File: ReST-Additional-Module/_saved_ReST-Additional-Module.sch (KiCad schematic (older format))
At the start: 11 parts, among them P1 CONN_02X06, P2 02-SCREW-TERM, P3 02-SCREW-TERM, Q1 Q_BSH105, Q2 Q_AOT240L

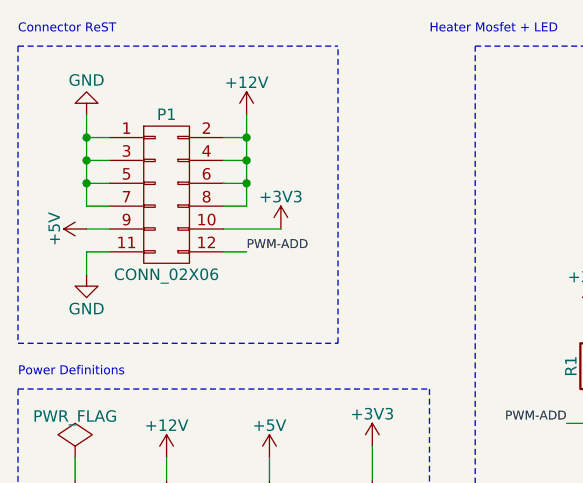
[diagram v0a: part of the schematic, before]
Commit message: Added Additional Module
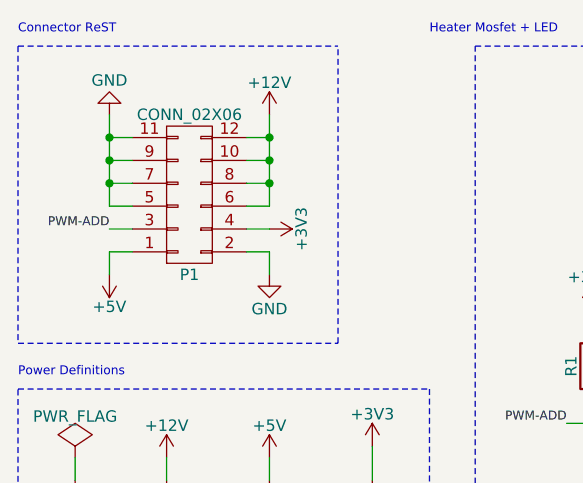
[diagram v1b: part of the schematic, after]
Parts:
- P1: footprint (none) -> Pin_Headers:Pin_Header_Angled_2x06
- P2: footprint 5mm-pitch-terminal:mkds_1,5-2 -> Pin_Headers:Pin_Header_Straight_1x02
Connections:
- net +12V: now also P1.10 (P10), P1.12 (P12); no longer P1.2 (P2), P1.4 (P4)
- net +3V3: now also P1.4 (P4); no longer P1.10 (P10)
- net +5V: now also P1.1 (P1); no longer P1.9 (P9)
- net GND: now also P1.2 (P2), P1.9 (P9); no longer P1.1 (P1), P1.3 (P3)
- net PWM-ADD: now also P1.3 (P3); no longer P1.12 (P12)
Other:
- moved on the sheet: P1
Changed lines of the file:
@@
 F 0 "P2" H 7350 2850 50  0000 C CNN
 F 1 "02-SCREW-TERM" V 7450 2700 50  0000 C CNN
-F 2 "5mm-pitch-terminal:mkds_1,5-2" H 7350 2700 50  0001 C CNN
+F 2 "Pin_Headers:Pin_Header_Straight_1x02" H 7350 2700 50  0001 C CNN
 F 3 "" H 7350 2700 50  0000 C CNN
 	1    7350 2700
@@
 $EndComp
 $Comp
-L +12V #PWR13
+L +12V #PWR01
 U 1 1 56A6924C
 P 6850 2350
-F 0 "#PWR13" H 6850 2200 50  0001 C CNN
+F 0 "#PWR01" H 6850 2200 50  0001 C CNN
 F 1 "+12V" H 6850 2490 50  0000 C CNN
 F 2 "" H 6850 2350 50  0000 C CNN
@@
 $EndComp
 $Comp
-L +5V #PWR3
+L +5V #PWR02
 U 1 1 56A6A1BB
-P 2950 2900
-F 0 "#PWR3" H 2950 2750 50  0001 C CNN
-F 1 "+5V" H 2950 3040 50  0000 C CNN
-F 2 "" H 2950 2900 50  0000 C CNN
-F 3 "" H 2950 2900 50  0000 C CNN
-	1    2950 2900
-	0    -1   -1   0
-$EndComp
-$Comp
-L +3V3 #PWR8
+P 3050 3100
+F 0 "#PWR02" H 3050 2950 50  0001 C CNN
+F 1 "+5V" H 3050 3240 50  0000 C CNN
+F 2 "" H 3050 3100 50  0000 C CNN
+F 3 "" H 3050 3100 50  0000 C CNN
+	1    3050 3100
+	-1   0    0    1
+$EndComp
+$Comp
+L +3V3 #PWR03
 U 1 1 56A6A1DD
-P 3800 2900
-F 0 "#PWR8" H 3800 2750 50  0001 C CNN
-F 1 "+3V3" H 3800 3040 50  0000 C CNN
-F 2 "" H 3800 2900 50  0000 C CNN
-F 3 "" H 3800 2900 50  0000 C CNN
-	1    3800 2900
-	1    0    0    -1
-$EndComp
-$Comp
-L GND #PWR4
+P 3750 2900
+F 0 "#PWR03" H 3750 2750 50  0001 C CNN
+F 1 "+3V3" H 3750 3040 50  0000 C CNN
+F 2 "" H 3750 2900 50  0000 C CNN
+F 3 "" H 3750 2900 50  0000 C CNN
+	1    3750 2900
+	0    1    1    0
+$EndComp
+$Comp
+L GND #PWR04
 U 1 1 56A6A1FF
-P 2950 3100
-F 0 "#PWR4" H 2950 2850 50  0001 C CNN
-F 1 "GND" H 2950 2950 50  0000 C CNN
-F 2 "" H 2950 3100 50  0000 C CNN
-F 3 "" H 2950 3100 50  0000 C CNN
-	1    2950 3100
-	1    0    0    -1
-$EndComp
-$Comp
-L GND #PWR14
+P 3750 3100
+F 0 "#PWR04" H 3750 2850 50  0001 C CNN
+F 1 "GND" H 3750 2950 50  0000 C CNN
+F 2 "" H 3750 3100 50  0000 C CNN
+F 3 "" H 3750 3100 50  0000 C CNN
+	1    3750 3100
+	1    0    0    -1
+$EndComp
+$Comp
+L GND #PWR05
 U 1 1 56A6B6EF
 P 6850 3850
-F 0 "#PWR14" H 6850 3600 50  0001 C CNN
+F 0 "#PWR05" H 6850 3600 50  0001 C CNN
 F 1 "GND" H 6850 3700 50  0000 C CNN
 F 2 "" H 6850 3850 50  0000 C CNN
@@
 $EndComp
 $Comp
-L +3V3 #PWR10
+L +3V3 #PWR06
 U 1 1 56A6D2B8
 P 5150 3250
-F 0 "#PWR10" H 5150 3100 50  0001 C CNN
+F 0 "#PWR06" H 5150 3100 50  0001 C CNN
 F 1 "+3V3" H 5150 3390 50  0000 C CNN
 F 2 "" H 5150 3250 50  0000 C CNN
@@
 $EndComp
 $Comp
-L +5V #PWR11
+L +5V #PWR07
 U 1 1 56A6D350
 P 5550 2750
-F 0 "#PWR11" H 5550 2600 50  0001 C CNN
+F 0 "#PWR07" H 5550 2600 50  0001 C CNN
 F 1 "+5V" H 5550 2890 50  0000 C CNN
 F 2 "" H 5550 2750 50  0000 C CNN
@@
 $EndComp
 $Comp
-L GND #PWR12
+L GND #PWR08
 U 1 1 56A6DF02
 P 5550 4050
-F 0 "#PWR12" H 5550 3800 50  0001 C CNN
+F 0 "#PWR08" H 5550 3800 50  0001 C CNN
 F 1 "GND" H 5550 3900 50  0000 C CNN
 F 2 "" H 5550 4050 50  0000 C CNN
@@
 Text Label 5050 3750 2    39   ~ 0
 PWM-ADD
-Text Label 3650 3000 0    39   ~ 0
+Text Label 3050 2900 2    39   ~ 0
 PWM-ADD
 $Comp
-L +12V #PWR5
+L +12V #PWR09
 U 1 1 56A7EB7B
 P 3300 3900
-F 0 "#PWR5" H 3300 3750 50  0001 C CNN
+F 0 "#PWR09" H 3300 3750 50  0001 C CNN
 F 1 "+12V" H 3300 4040 50  0000 C CNN
 F 2 "" H 3300 3900 50  0000 C CNN
@@
 $EndComp
 $Comp
-L GND #PWR1
+L GND #PWR010
 U 1 1 56A7EBB6
 P 2900 4000
-F 0 "#PWR1" H 2900 3750 50  0001 C CNN
+F 0 "#PWR010" H 2900 3750 50  0001 C CNN
 F 1 "GND" H 2900 3850 50  0000 C CNN
 F 2 "" H 2900 4000 50  0000 C CNN
@@
 $EndComp
 $Comp
-L +5V #PWR7
+L +5V #PWR011
 U 1 1 56A7EBF1
 P 3750 3900
-F 0 "#PWR7" H 3750 3750 50  0001 C CNN
+F 0 "#PWR011" H 3750 3750 50  0001 C CNN
 F 1 "+5V" H 3750 4040 50  0000 C CNN
 F 2 "" H 3750 3900 50  0000 C CNN
@@
 $EndComp
 $Comp
-L +3V3 #PWR9
+L +3V3 #PWR012
 U 1 1 56A7EC2C
 P 4200 3850
-F 0 "#PWR9" H 4200 3700 50  0001 C CNN
+F 0 "#PWR012" H 4200 3700 50  0001 C CNN
 F 1 "+3V3" H 4200 3990 50  0000 C CNN
 F 2 "" H 4200 3850 50  0000 C CNN
@@
 $EndComp
 $Comp
-L PWR_FLAG #FLG4
+L PWR_FLAG #FLG013
 U 1 1 56A7EC59
 P 4200 4000
-F 0 "#FLG4" H 4200 4095 50  0001 C CNN
+F 0 "#FLG013" H 4200 4095 50  0001 C CNN
 F 1 "PWR_FLAG" H 4200 4180 50  0000 C CNN
 F 2 "" H 4200 4000 50  0000 C CNN
@@
 $EndComp
 $Comp
-L PWR_FLAG #FLG3
+L PWR_FLAG #FLG014
 U 1 1 56A7EC9B
 P 3750 4000
-F 0 "#FLG3" H 3750 4095 50  0001 C CNN
+F 0 "#FLG014" H 3750 4095 50  0001 C CNN
 F 1 "PWR_FLAG" H 3750 4180 50  0000 C CNN
 F 2 "" H 3750 4000 50  0000 C CNN
@@
 $EndComp
 $Comp
-L PWR_FLAG #FLG2
+L PWR_FLAG #FLG015
 U 1 1 56A7ECD6
 P 3300 4000
-F 0 "#FLG2" H 3300 4095 50  0001 C CNN
+F 0 "#FLG015" H 3300 4095 50  0001 C CNN
 F 1 "PWR_FLAG" H 3300 4180 50  0000 C CNN
 F 2 "" H 3300 4000 50  0000 C CNN
@@
 $EndComp
 $Comp
-L PWR_FLAG #FLG1
+L PWR_FLAG #FLG016
 U 1 1 56A7ED11
 P 2900 3900
-F 0 "#FLG1" H 2900 3995 50  0001 C CNN
+F 0 "#FLG016" H 2900 3995 50  0001 C CNN
 F 1 "PWR_FLAG" H 2900 4080 50  0000 C CNN
 F 2 "" H 2900 3900 50  0000 C CNN
@@
 Power Definitions
 $Comp
-L +12V #PWR6
+L +12V #PWR017
 U 1 1 56AC08E7
-P 3650 2400
-F 0 "#PWR6" H 3650 2250 50  0001 C CNN
-F 1 "+12V" H 3650 2540 50  0000 C CNN
-F 2 "" H 3650 2400 50  0000 C CNN
-F 3 "" H 3650 2400 50  0000 C CNN
-	1    3650 2400
-	1    0    0    -1
-$EndComp
-$Comp
-L GND #PWR2
+P 3750 2400
+F 0 "#PWR017" H 3750 2250 50  0001 C CNN
+F 1 "+12V" H 3750 2540 50  0000 C CNN
+F 2 "" H 3750 2400 50  0000 C CNN
+F 3 "" H 3750 2400 50  0000 C CNN
+	1    3750 2400
+	1    0    0    -1
+$EndComp
+$Comp
+L GND #PWR018
 U 1 1 56AC091C
-P 2950 2400
-F 0 "#PWR2" H 2950 2150 50  0001 C CNN
-F 1 "GND" H 2950 2250 50  0000 C CNN
-F 2 "" H 2950 2400 50  0000 C CNN
-F 3 "" H 2950 2400 50  0000 C CNN
-	1    2950 2400
+P 3050 2400
+F 0 "#PWR018" H 3050 2150 50  0001 C CNN
+F 1 "GND" H 3050 2250 50  0000 C CNN
+F 2 "" H 3050 2400 50  0000 C CNN
+F 3 "" H 3050 2400 50  0000 C CNN
+	1    3050 2400
 	-1   0    0    1
 $EndComp
@@
 L CONN_02X06 P1
 U 1 1 56AD3C5B
-P 3300 2750
-F 0 "P1" H 3300 3100 50  0000 C CNN
-F 1 "CONN_02X06" H 3300 2400 50  0000 C CNN
-F 2 "" H 3300 1550 50  0000 C CNN
-F 3 "" H 3300 1550 50  0000 C CNN
-	1    3300 2750
-	1    0    0    -1
-$EndComp
-Wire Wire Line
-	3650 2400 3650 2800
-Wire Wire Line
-	3650 2500 3550 2500
-Wire Wire Line
-	3650 2600 3550 2600
-Connection ~ 3650 2500
-Wire Wire Line
-	3650 2700 3550 2700
-Connection ~ 3650 2600
-Wire Wire Line
-	3650 2800 3550 2800
-Connection ~ 3650 2700
-Wire Wire Line
-	2950 2400 2950 2800
-Wire Wire Line
-	2950 2500 3050 2500
-Wire Wire Line
-	2950 2600 3050 2600
-Connection ~ 2950 2500
-Wire Wire Line
-	2950 2700 3050 2700
-Connection ~ 2950 2600
-Wire Wire Line
-	2950 2800 3050 2800
-Connection ~ 2950 2700
-Wire Wire Line
-	2950 2900 3050 2900
-Wire Wire Line
-	3550 2900 3800 2900
-Wire Wire Line
-	3050 3000 2950 3000
-Wire Wire Line
-	2950 3000 2950 3100
-Wire Wire Line
-	3650 3000 3550 3000
+P 3400 2750
+F 0 "P1" H 3400 3100 50  0000 C CNN
+F 1 "CONN_02X06" H 3400 2400 50  0000 C CNN
+F 2 "Pin_Headers:Pin_Header_Angled_2x06" H 3400 1550 50  0001 C CNN
+F 3 "" H 3400 1550 50  0000 C CNN
+	1    3400 2750
+	1    0    0    1
+$EndComp
+Wire Wire Line
+	3750 2400 3750 2800
+Wire Wire Line
+	3750 2500 3650 2500
+Wire Wire Line
+	3750 2600 3650 2600
+Connection ~ 3750 2500
+Wire Wire Line
+	3750 2700 3650 2700
+Connection ~ 3750 2600
+Wire Wire Line
+	3750 2800 3650 2800
+Connection ~ 3750 2700
+Wire Wire Line
+	3050 2400 3050 2800
+Wire Wire Line
+	3050 2500 3150 2500
+Wire Wire Line
+	3050 2600 3150 2600
+Connection ~ 3050 2500
+Wire Wire Line
+	3050 2700 3150 2700
+Connection ~ 3050 2600
+Wire Wire Line
+	3050 2800 3150 2800
+Connection ~ 3050 2700
 Wire Notes Line
 	2650 2100 4050 2100
@@
 Wire Notes Line
 	4050 3400 4050 2100
+Wire Wire Line
+	3750 2900 3650 2900
+Wire Wire Line
+	3150 2900 3050 2900
+Wire Wire Line
+	3050 3100 3050 3000
+Wire Wire Line
+	3050 3000 3150 3000
+Wire Wire Line
+	3650 3000 3750 3000
+Wire Wire Line
+	3750 3000 3750 3100
 $EndSCHEMATC
